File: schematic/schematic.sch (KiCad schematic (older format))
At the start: 2 parts

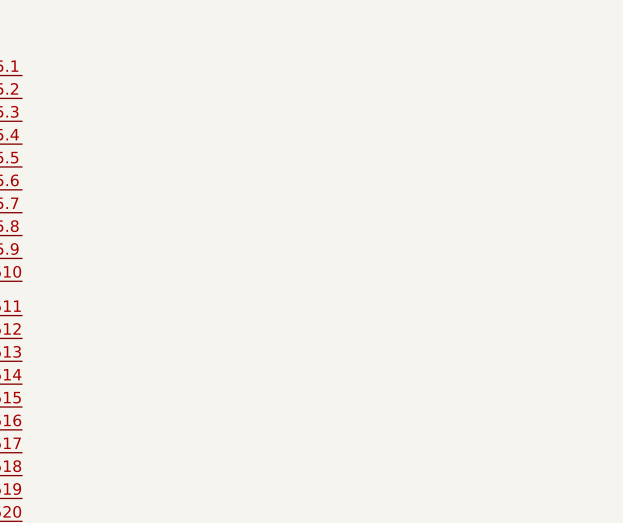
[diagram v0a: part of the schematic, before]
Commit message: schematic - camera
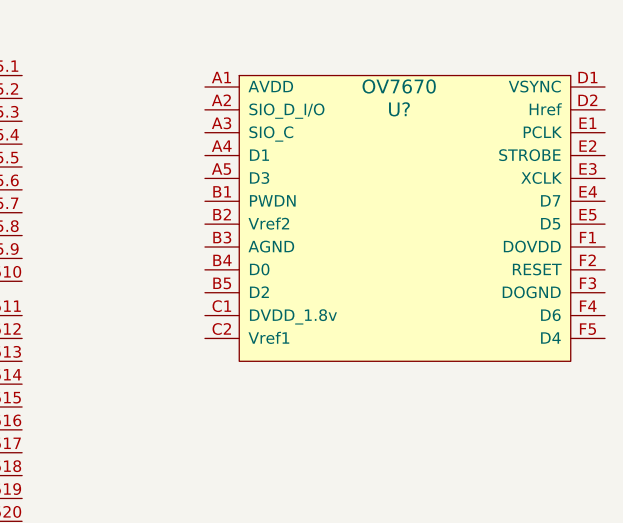
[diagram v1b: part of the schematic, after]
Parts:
- added U?: OV7670, symbol OV7670
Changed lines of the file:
@@
+	1    0    0    -1
+$EndComp
+$Comp
+L OV7670 U?
+U 1 1 58CA1507
+P 8400 3000
+F 0 "U?" H 8400 2750 60  0000 C CNN
+F 1 "OV7670" H 8400 2850 60  0000 C CNN
+F 2 "" H 8400 3000 60  0000 C CNN
+F 3 "" H 8400 3000 60  0000 C CNN
+	1    8400 3000
 	1    0    0    -1
 $EndComp

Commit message: half finished wiring
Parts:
- added BT? (x2): Battery, symbol Battery
- added Q?: BUZ11, TO-220, symbol BUZ11
- added Q? (x2): MMBT3904, SOT-23, symbol MMBT3904
- added R? (x5): R, symbol R
- added R?: Photores, symbol Photores
- added TH?: THERMISTOR, symbol THERMISTOR
- added U?: LPS331AP, symbol LPS331AP
- added U?: GP-20U7, symbol GP-20U7
- added U? (x3): 3.6V, symbol 3.6V
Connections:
- net at U?.J1.2 (P6.5): now also Q?.2 (G)
- net at U?.J1.3 (P3.4/UCA0RXD): now also U?.3 (Tx), U?.~ (vcc)
- net at U?.J1.4 (P3.3/UCA0TXD): now also U?.2 (Rx), U?.~ (vcc)
- net at U?.J1.6 (P6.6): now also U?.13 (ON/sleep/DIO9)
- net at U?.J1.7 (P3.2/UCA0STE): now also U?.12 (CTS/DIO7)
- net at U?.J1.8 (P2.7): now also U?.11 (INT1)
- net at U?.J113 (P6.0): now also U?.B1 (PWDN)
- net at U?.J114 (P6.1): now also Q?.1 (B)
- net at U?.J115 (P6.2): now also Q?.1 (B)
- net servo_pwm: now reaches U?.J116 (P6.3)
- net at U?.J117 (P6.4): now also U?.9 (DTR/Sleep/DIO8)
- net at U?.J118 (P7.0/ADC12): now also R?.1, R?.2, TH?.2
- net at U?.J5.1 (P2.5): now also U?.F5 (D4)
- net at U?.J5.2 (P2.4): now also U?.A5 (D3)
- net at U?.J5.3 (P1.5): now also U?.F4 (D6)
- net at U?.J5.4 (P1.4): now also U?.E4 (D7)
- net at U?.J512 (P2.0): now also U?.B4 (D0)
- net at U?.J513 (P2.2): now also U?.A4 (D1)
- net at U?.J516 (P3.0/UCB0SDA): now also U?.A2 (SIO_D_I/O), U?.6 (SDA/SDI/SDO)
- net at U?.J517 (P3.1/UCB0SCL): now also U?.A3 (SIO_C), U?.4 (SCL/SPC)
- net at U?.J518 (P2.6): now also U?.E5 (D5)
- net at U?.J519 (P2.3): now also U?.B5 (D2)
- net +3V3: now reaches U?.1 (Vcc)
- net +3V3: now also Q?.3 (C), Q?.3 (C), R?.1, R?.2
- net GND: now reaches U?.10 (GND)
- net GND: now also BT?.2, BT?.2, R?.2, R?.2
- new net: BT?.1, R?.1, U?.~
- new net: Q?.2 (E), TH?.1
- new net: Q?.2 (E), R?.1
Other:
- note added: "periph_pwr"
- moved on the sheet: U?

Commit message: updated schematic
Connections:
- net at U?.3 (Tx), U?.J1.3 (P3.4/UCA0RXD): no longer U?.~ (vcc)
- net at U?.2 (Rx), U?.J1.4 (P3.3/UCA0TXD): no longer U?.~ (vcc)
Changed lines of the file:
@@
 Connection ~ 6850 4650
-Wire Wire Line
-	3200 2150 3200 3400
-Connection ~ 3200 3400
-Wire Wire Line
-	3300 2150 3300 3300
-Connection ~ 3300 3300
 Wire Wire Line
 	4950 4750 4150 4750

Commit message: stuff from sun 4/2
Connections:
- net servo_pwm: no longer names the net of U?.J116 (P6.3)
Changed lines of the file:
@@
 $EndComp
 Wire Wire Line
-	1400 800  1400 850
-Wire Wire Line
-	1400 850  1400 950
+	1400 800  1400 950
 Wire Wire Line
 	2950 5150 3950 5150
@@
 	1000 4550 1000 3400
 Wire Wire Line
-	1000 3400 3200 3400
-Wire Wire Line
-	3200 3400 4950 3400
-Wire Wire Line
-	900  3300 3300 3300
-Wire Wire Line
-	3300 3300 4950 3300
+	1000 3400 4950 3400
+Wire Wire Line
+	900  3300 4950 3300
 Wire Wire Line
 	900  3300 900  4650
@@
 	4050 5250 2950 5250
 Wire Wire Line
-	6750 4750 6950 4750
-Wire Wire Line
-	6950 4750 7450 4750
+	6750 4750 7450 4750
 Wire Wire Line
 	7450 4750 7450 3300
@@
 	7550 3200 7350 3200
 Wire Wire Line
-	7350 3200 7350 4650
-Wire Wire Line
-	7350 4650 6850 4650
-Wire Wire Line
-	6850 4650 6750 4650
+	7350 4650 7350 3200
+Wire Wire Line
+	6750 4650 7350 4650
 Wire Wire Line
 	6750 4250 7250 4250
@@
 Connection ~ 1400 850
 Wire Wire Line
-	2100 1150 2100 1250
-Wire Wire Line
-	2100 1250 2100 1300
+	2100 1150 2100 1300
 $Comp
 L GND #PWR?
@@
 	5850 5700 5850 5800
 Wire Wire Line
-	5350 5800 5850 5800
-Wire Wire Line
-	5850 5800 6250 5800
+	5350 5800 6250 5800
 Wire Wire Line
 	5350 5800 5350 6050
@@
 	5350 6950 5350 7150
 Wire Wire Line
-	4550 7150 5350 7150
-Wire Wire Line
-	5350 7150 5800 7150
-Wire Wire Line
-	5800 7150 6250 7150
+	4550 7150 6250 7150
 Wire Wire Line
 	6250 7150 6250 6950
@@
 $EndComp
 Wire Wire Line
-	4950 4650 4200 4650
-Text Label 4200 4650 0    60   ~ 0
-servo_pwm
+	4950 5050 4250 5050
+Wire Wire Line
+	4250 5050 4250 6600
+Wire Wire Line
+	4250 6600 3100 6600
+Wire Wire Line
+	3100 6600 3100 6950
 $EndSCHEMATC
